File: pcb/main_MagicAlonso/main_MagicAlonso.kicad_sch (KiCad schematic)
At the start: 14 parts, among them J1 XT30PW-M, SW1 SW_SPST, U1 ESP32-WROOM-32E, U2 Mini360, U3 LM1117DT-3.3

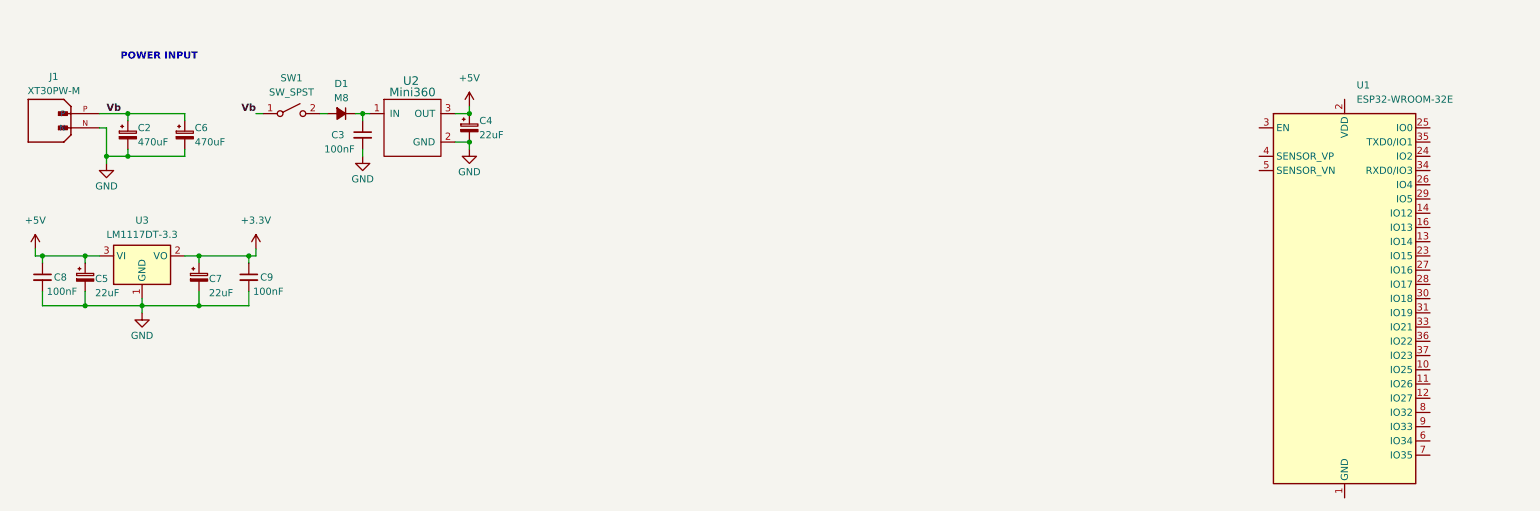
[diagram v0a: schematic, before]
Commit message: Schematic & PCB updates
made advancements on the schematic circuits and the PCB layout drawings.
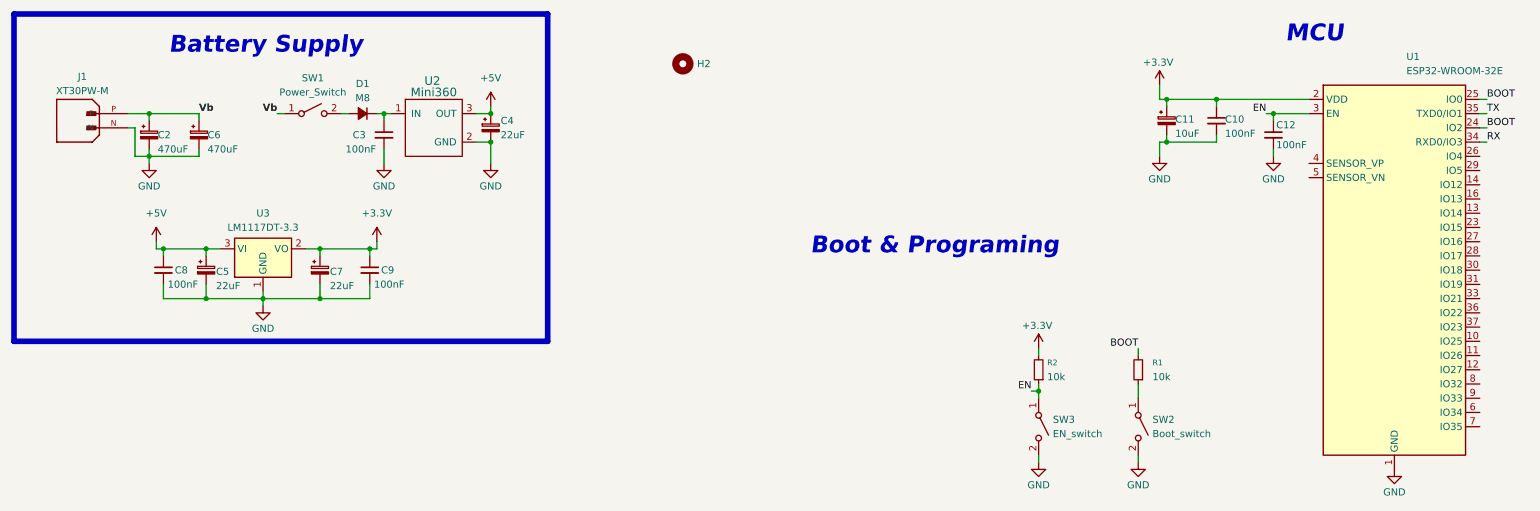
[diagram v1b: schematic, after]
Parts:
- added C10, C12: 100nF, symbol Device:C_Small
- added C11: 10uF, symbol Device:C_Polarized_Small
- added H2: Mounting_Hole, EESTN5:hole_3mm, symbol EESTN5:Mounting_Hole
- added R1, R2: 10k, symbol Device:R_Small
- added SW2: Boot_switch, MixLib:SW_Slide-03_P2.54_L9_W4_H7, symbol Switch:SW_SPST
- added SW3: EN_switch, MixLib:SW_Slide-03_P2.54_L9_W4_H7, symbol Switch:SW_SPST
- SW1: value SW_SPST -> Power_Switch; footprint (none) -> MixLib:SW_Slide-03_P2.54_L9_W4_H7
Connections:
- net +3.3V: now also U1.2 (VDD), C10.1, C11.1, R2.2
- net GND: now also U1.1 (GND), U1.15 (GND), U1.38 (GND), U1.39 (GND), C10.2, C11.2, C12.2, SW2.2 (B), SW3.2 (B)
- net BOOT: now reaches U1.24 (IO2)
- net BOOT: now also U1.25 (IO0), R1.2
- net EN: now reaches U1.3 (EN)
- net EN: now also C12.1, R2.1, SW3.1 (A)
- net RX: now reaches U1.34 (RXD0/IO3)
- net TX: now reaches U1.35 (TXD0/IO1)
- new net: R1.1, SW2.1 (A)
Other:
- note added: "Battery Supply"
- note added: "Boot & Programing"
- note added: "MCU"
- note removed: "POWER INPUT"
- moved on the sheet: C2, C3, C4, C5, C6, C7, C8, C9, D1, J1, SW1, U1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

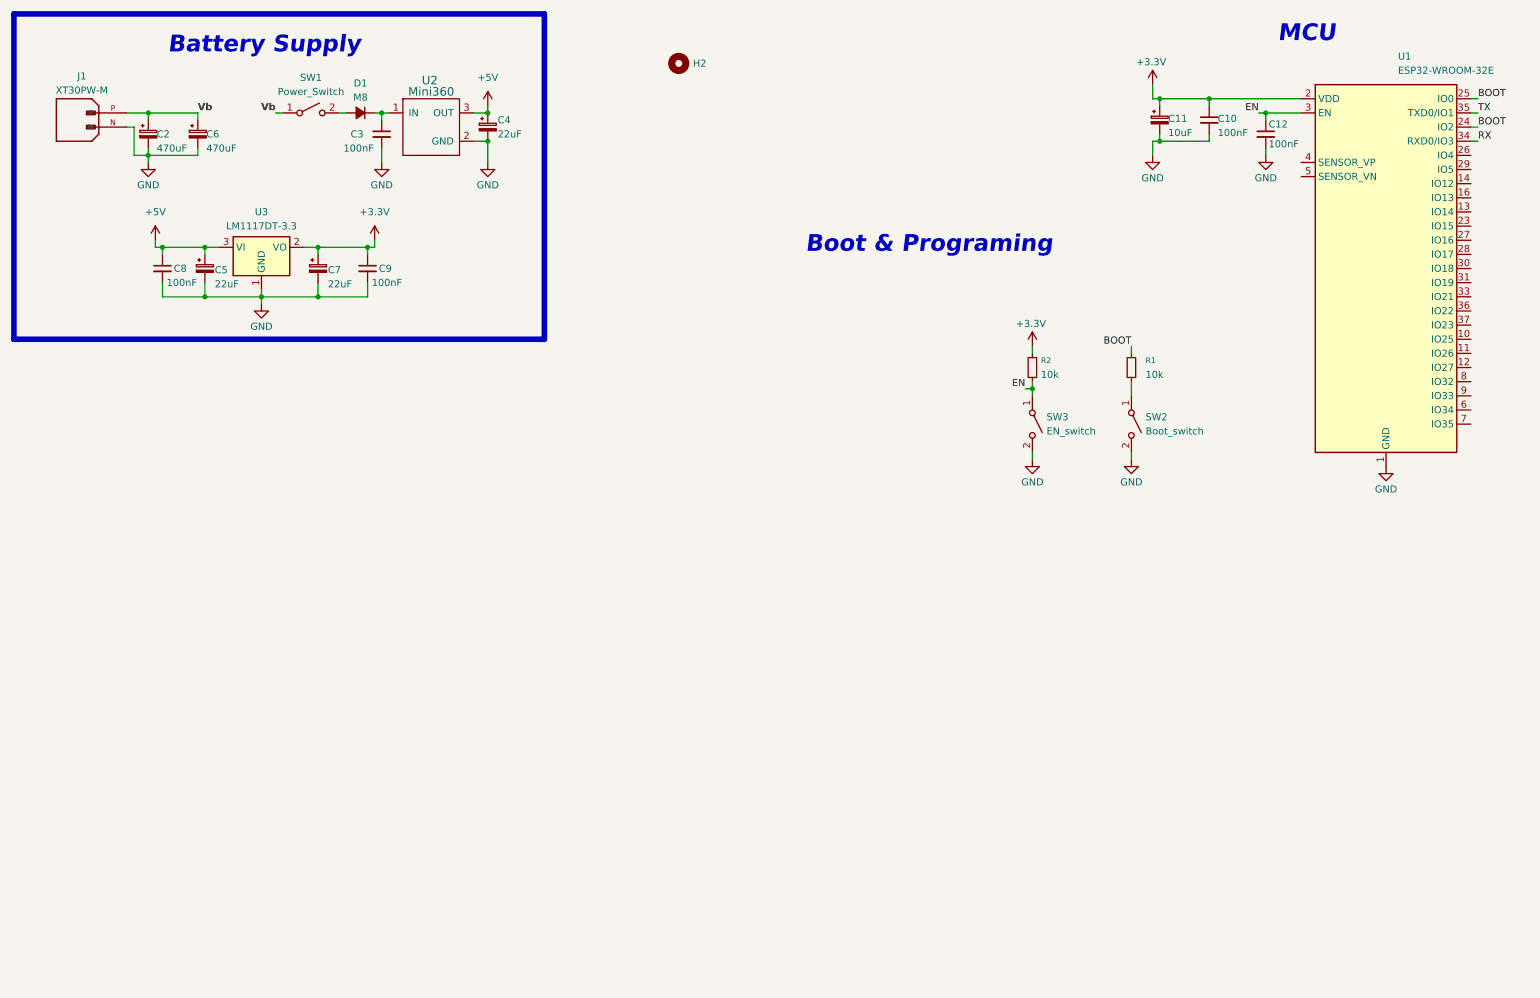
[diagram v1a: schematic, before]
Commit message: more schematic stuff
Added ch340 and some more stuff
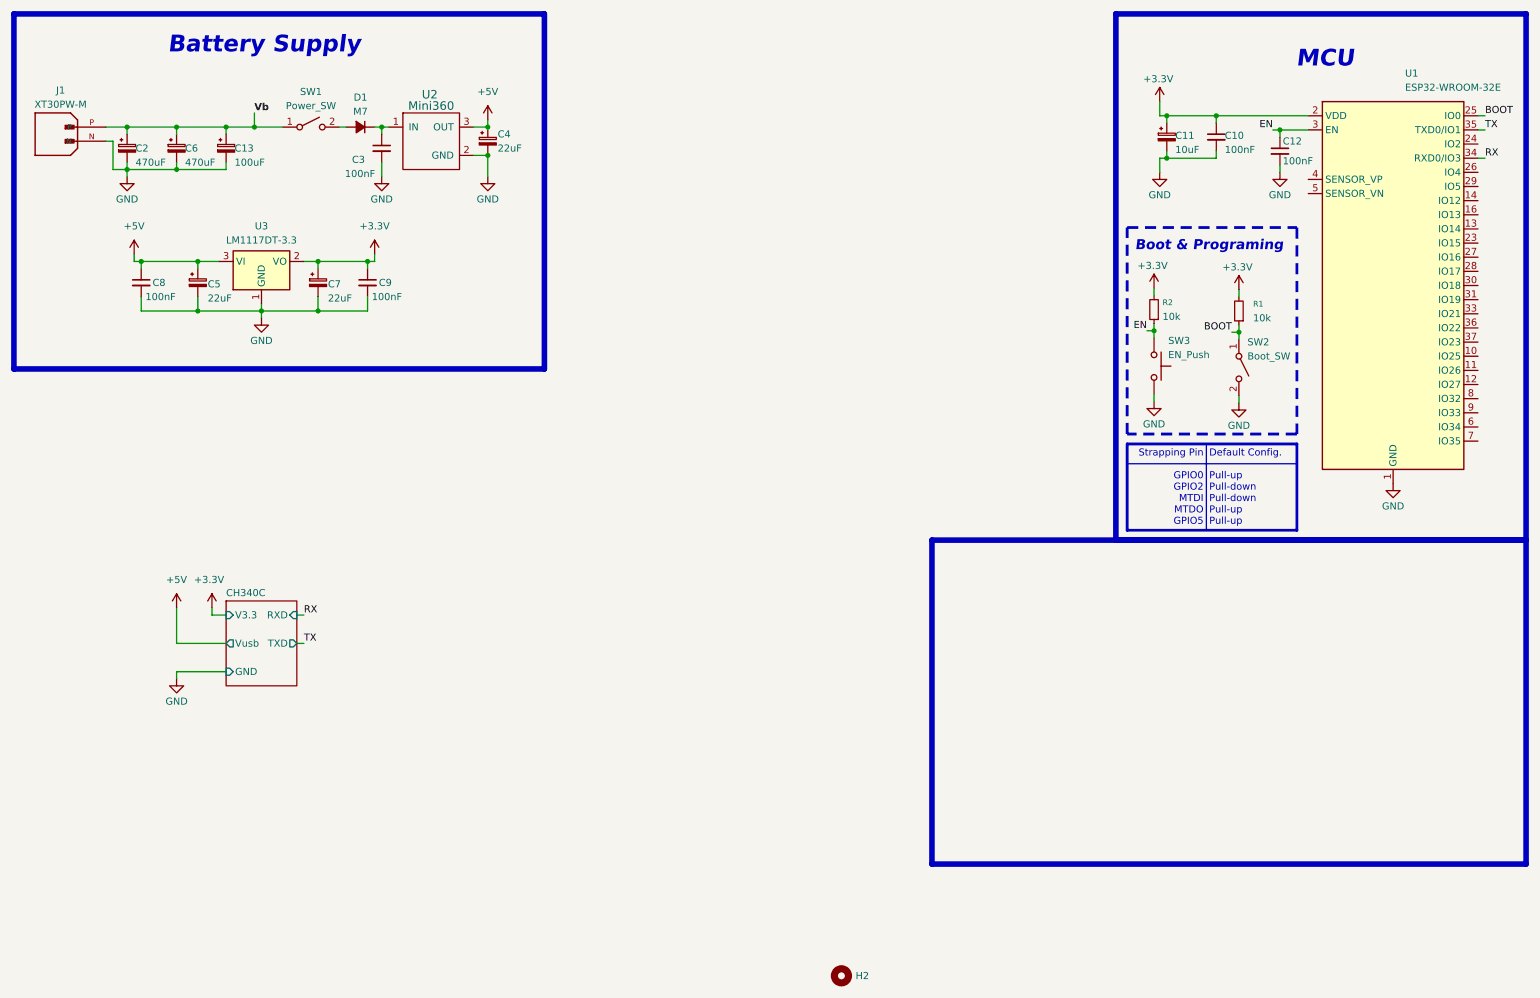
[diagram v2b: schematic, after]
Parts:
- removed SW3: EN_switch, MixLib:SW_Slide-03_P2.54_L9_W4_H7, symbol Switch:SW_SPST
- added C13: 100uF, symbol Device:C_Polarized_Small
- added SW3: EN_Push, symbol Switch:SW_Push
- D1: value M8 -> M7
- SW1: value Power_Switch -> Power_SW
- SW2: value Boot_switch -> Boot_SW
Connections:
- net +3.3V: now also R1.2
- net BOOT: now also R1.1, SW2.1 (A); no longer R1.2, U1.24 (IO2)
- net EN: now also SW3.1
- net GND: now also C13.2, SW3.2
- net Vb: now also C13.1
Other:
- added sheet CH340C (CH340G_programmer.kicad_sch)
- note added: "Default Config. Pull-up Pull-down Pull-down Pull-up Pull-up"
- note added: "Strapping Pin GPIO0 GPIO2 MTDI MTDO GPIO5"
- company: (none) -> JRegi
- title: (none) -> MagicAlonso main control PCB
- moved on the sheet: C10, C11, C12, C2, C3, C4, C5, C6, C7, C8, C9, D1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

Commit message: more schematic
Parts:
- added C17, C18, C19, C20, C21, C22, C23, C24, C25, C26, C27, C28, C29, C30, C31, C32: 100nF, symbol Device:C_Small
- added J5, J6: Conn_01x08_Pin, symbol Connector:Conn_01x08_Pin
- added JP1: JP_ESP, symbol Jumper:SolderJumper_2_Open
- added U5: CD74HC4067, MixLib:HP4067_module, symbol MixLib:CD74HC4067_module
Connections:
- net +3.3V: now also JP1.2 (B); no longer C10.1, C11.1, U1.2 (VDD)
- net GND: now also C17.1, C18.1, C19.1, C20.1, C21.1, C22.1, C23.1, C24.1, C25.1, C26.1, C27.1, C28.1, C29.1, C30.1, C31.1, C32.1, U5.24 (GND)
- net MUX_S1: now reaches U1.6 (IO34)
- net MUX_S1: now also U5.20 (S1)
- net MUX_S0: now reaches U1.7 (IO35)
- net MUX_S0: now also U5.21 (S0)
- net MUX_SIG: now reaches U1.8 (IO32)
- net MUX_SIG: now also U5.17 (SIG)
- new net: C10.1, C11.1, JP1.1 (A), U1.2 (VDD)
- new net MUX_S2: U5.19 (S2)
- new net MUX_S3: U5.18 (S3)
- new net QRE_0: C32.2, J6.8 (Pin_8), U5.16 (C0)
- new net QRE_1: C31.2, J6.7 (Pin_7), U5.15 (C1)
- new net QRE_10: C22.2, J5.6 (Pin_6), U5.6 (C10)
- new net QRE_11: C21.2, J5.5 (Pin_5), U5.5 (C11)
- new net QRE_12: C20.2, J5.4 (Pin_4), U5.4 (C12)
- new net QRE_13: C19.2, J5.3 (Pin_3), U5.3 (C13)
- new net QRE_14: C18.2, J5.2 (Pin_2), U5.2 (C14)
- new net QRE_15: C17.2, J5.1 (Pin_1), U5.1 (C15)
- new net QRE_2: C30.2, J6.6 (Pin_6), U5.14 (C2)
- new net QRE_3: C29.2, J6.5 (Pin_5), U5.13 (C3)
- new net QRE_4: C28.2, J6.4 (Pin_4), U5.12 (C4)
- new net QRE_5: C27.2, J6.3 (Pin_3), U5.11 (C5)
- new net QRE_6: C26.2, J6.2 (Pin_2), U5.10 (C6)
- new net QRE_7: C25.2, J6.1 (Pin_1), U5.9 (C7)
- new net QRE_8: C24.2, J5.8 (Pin_8), U5.8 (C8)
- new net QRE_9: C23.2, J5.7 (Pin_7), U5.7 (C9)
- no-connect marks 0 -> 1
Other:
- note added: "Boot"
- note added: "MUX & Sensors Output"
- note added: "Programming"
- note added: "To-Do - MUX y conexion sensores - giroscopio y acelerometro - encoders - usb-c symbol & footprint - buzzer - 2 LEDs RGB - 1 interface button - mounting holes - ESC connections"
- note removed: "Boot & Programing"
- moved on the sheet: C10, C11, C12, R1, R2, SW2, SW3, U1

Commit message: yes, schematic
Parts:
- added C33, C34: 100nF, symbol Device:C_Small
- C5, C7: value 22uF -> 47uF
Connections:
- net BOOT: now also C34.1
- net EN: now also C33.1
- net GND: now also C33.2, C34.2
- net VDD_ESP: now reaches C10.1, C11.1, JP1.1 (A), U1.2 (VDD)
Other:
- note added: "Interfaces"
- note added: "To-Do - giroscopio y acelerometro - encoders - usb-c symbol & footprint - buzzer - 2 LEDs RGB - 1 interface button - mounting holes - ESC connections"
- note removed: "To-Do - MUX y conexion sensores - giroscopio y acelerometro - encoders - usb-c symbol & footprint - buzzer - 2 LEDs RGB - 1 interface button - mounting holes - ESC connections"
- moved on the sheet: C13, C17, C18, C19, C2, C20, C21, C22, C23, C24, C25, C26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

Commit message: hehe schematic go brr
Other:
- note added: "To-Do - giroscopio y acelerometro - encoders - usb-c symbol & footprint - buzzer - 2 LEDs RGB - 1 interface button - mounting holes - ESC connections - quizas integrar step-down"
- note removed: "To-Do - giroscopio y acelerometro - encoders - usb-c symbol & footprint - buzzer - 2 LEDs RGB - 1 interface button - mounting holes - ESC connections"
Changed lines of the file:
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@@
 		)
 	)
-	(text "To-Do\n- giroscopio y acelerometro\n- encoders\n- usb-c symbol & footprint\n- buzzer\n- 2 LEDs RGB\n- 1 interface button\n- mounting holes\n- ESC connections\n"
+	(text "To-Do\n- giroscopio y acelerometro\n- encoders\n- usb-c symbol & footprint\n- buzzer\n- 2 LEDs RGB\n- 1 interface button\n- mounting holes\n- ESC connections\n- quizas integrar step-down\n"
 		(exclude_from_sim no)
 		(at -114.046 85.598 0)
@@
 			"agA0ACsAbQBrAHcAbgB3AGYAdQBVAHMAcQBrAFIATQB4AE8AYgBTAEgAQQArAHAANQB4AEYARQBk"
 			"AG4ANwBzAEoAbABKAEsASgBGAG8AWgBtAFkAVwBVAHcASwB6AEkAbABBAHQAcgByAGgARgBBAEQA"
-			"dQBmAA=="
+			"dQBmAHoAKwBlAHoAVwBRAGgAQgBzAHUAUwBVAFYAcQB1AFYAOQA1AHgARgBSAEQAVgBVAG8AUQBx"
+			"AGgAYgB1AHEAYwBrAHEAaABlAHUASABEAGgAOAByAFcAcgBKAGUASABlAHEAVABhAGgAUABuAC8A"
+			"dQAvAE8ASABoAGcAWQBpAHEAVwB1AEgAQgB5AHgAUwBGAHEAYQBsAEMAVgBWAFYASABSAC8ATwBj"
+			"AFUAcgAvAHUAbQBxAFoAQgBwAG4ANwBvAGMAOQA3AFkATABoAFQAegBXAFYAQQBwAGcAVgBLAEEA"
+			"QgBBAHkARgA0AGsAUQBFADUAbwAxAGwAUgB3AG0ATwBvADUAMgBGAEIANABCAHoAbgBvAGwAeQB6"
+			"AEQAbABuAFkAaQA3ADkARgAwAEMATABZAEgAawA3AEkASgBRAC8AYgBnAFIARABFAFoARwBaADUA"
+			"bQB6AGIAUgBVAFIAawBSAEgAUgBsADIAdwBhADIARgBhAEkAQwBBAEsAQQBoAGIAQQBlAFIAagBV"
+			"AHMASQBBAEoASQBaADUASQB6ADkASQBCADYAWQBGAFUAVQBNADAAQQBSAFEAbQBRAHgANQBGAE8A"
+			"eABHAFAAVgAwAFAASwBhAHYANwBOAE4ATgB5AEwAMwByAFIAaQArADYANgA2ADYANQA3ADcANwAy"
+			"ADMATABQADcAOAB6AC8ALwA4AHIALwB6AEsAcgAzAFIAZAA5ADUAYQAzAHYARwBYADMAbgBtAGMA"
+			"OQA2ADEAbABmACsANwBWAGYAdQA3AC8AQgAyAEcATwBQAFAAZgBiAFkAWQA0ADgAOQBoAGIAcgBI"
+			"AEgAbgB2AHMAcwBjAGMAZQBlADMAdwBSAEkAVwBmADUAeABMADIAWABQAC8AcgB4AEsAMQBXAG8A"
+			"UQBOAEgAVQBSAEIASwBBAEEAQgBJAGcAQQAzAEwASgBiAEYAbQB2ADEANgB2AFYAZQByAEYAYwBU"
+			"AEIAZQB6AGcANABPAEQAKwBYAHgAZQBOAFgAVgBkADEAUQBRAG8AbwBwAHAAVAA0ADMAbgBvAE8A"
+			"ZwBJAG8ARABvAGsAYgBYADEATQBpAEoAQQBSAEMAQgBpAFEARQBSAGwASgBWADAAVQBRAEEAbABu"
+			"AFAASgB0AFMAOABpAE0AdABpAFMASABVAGgAawBXAC8ANgAwAEUAQgBoAEUAcQBBAG8AUAB0ADYA"
+			"egBkAHMASABUAE0AWABLAHgATABOAHcANgBHAFYASgBLADcAdwBVAFMASwBPAGoATABGAEMAQQBC"
+			"AEYARwA3AHYASgBQAEMASQBpAHAAQwAxADMAeQBwAHUANgA2AFgASABvAGgAMABIAE4AaQBIAGcA"
+			"MgBtAA=="
 		)
 	)

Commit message: schematic go fiuuu
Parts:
- removed C13: 100uF, symbol Device:C_Polarized_Small
- removed C4: 22uF, symbol Device:C_Polarized_Small
- added C35, C39, C40: 100nF, symbol Device:C_Small
- added C36, C37: 47uF, symbol Device:C_Polarized_Small
- C2: value 470uF -> 220uF
- C5, C7: value 47uF -> 22uF
- C6: value 470uF -> 100uF
- J5: value Conn_01x08_Pin -> QRE_Conn1
- J6: value Conn_01x08_Pin -> QRE_Conn2
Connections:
- net +5V: now also C35.1, C36.1
- net GND: now also C35.2, C36.2, C37.2, C39.1, C40.1
- net MUX_SIG: now also C39.2, C40.2
- net at C3.1, D1.1 (K), U2.1 (IN): now also C37.1
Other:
- note added: "To-Do - giroscopio y acelerometro - encoders - usb-c symbol & footprint - buzzer - 2 LEDs RGB - 1 interface button - DIP Switch 2 vias - mounting holes - ESC connections - quizas integrar step-down"
- note removed: "To-Do - giroscopio y acelerometro - encoders - usb-c symbol & footprint - buzzer - 2 LEDs RGB - 1 interface button - mounting holes - ESC connections - quizas integrar step-down"
- moved on the sheet: C17, C18, C19, C20, C21, C22, C23, C24, C25, C26, C27, C28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

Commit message: esquematico
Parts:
- removed C17, C18, C19, C20, C21, C22, C23, C24, C25, C26, C27, C28, C29, C30, C31, C32, C39, C40: 100nF, symbol Device:C_Small
- added C13: 1uF, symbol Device:C_Polarized_Small
- added C38: 100nF, symbol Device:C_Small
- added R7: 10k, symbol Device:R_Small
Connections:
- net +3.3V: now also U5.23 (VCC), C13.1, C38.1
- net GND: now also C13.2, C38.2, R7.1
- net MUX_SIG: now also R7.2
- net +5V renamed +4.3
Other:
- moved on the sheet: C3, C35, C36, C37, C5, C7, C8, C9, D1, SW1, U2, U3

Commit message: esquematico
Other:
- note added: "To-Do - giroscopio y acelerometro - encoders - usb module footprint - buzzer - 2 ws2822b smd - 1 interface button - DIP Switch 2 vias ?? - mounting holes - ESC connections - quizas integrar step-down - soldar modulo de MUX como Modulo SMD - Sensores de corriente"
- note removed: "To-Do - giroscopio y acelerometro - encoders - usb-c symbol & footprint - buzzer - 2 LEDs RGB - 1 interface button - DIP Switch 2 vias - mounting holes - ESC connections - quizas integrar step-down"
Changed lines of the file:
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@@
 		)
 	)
-	(text "To-Do\n- giroscopio y acelerometro\n- encoders\n- usb-c symbol & footprint\n- buzzer\n- 2 LEDs RGB\n- 1 interface button\n- DIP Switch 2 vias\n- mounting holes\n- ESC connections\n- quizas integrar step-down\n"
+	(text "To-Do\n- giroscopio y acelerometro\n- encoders\n- usb module footprint\n- buzzer\n- 2 ws2822b smd\n- 1 interface button\n- DIP Switch 2 vias ??\n- mounting holes\n- ESC connections\n- quizas integrar step-down\n- soldar modulo de MUX como Modulo SMD\n- Sensores de corriente"
 		(exclude_from_sim no)
-		(at -114.046 85.598 0)
+		(at -167.894 75.184 0)
 		(effects
 			(font
@@
 	(text "Interfaces"
 		(exclude_from_sim no)
-		(at 146.05 142.494 0)
+		(at 129.794 142.748 0)
 		(effects
 			(font
@@
 			"RAA5AHgAMgAyADAAVwBvADEAaQB1AHYAdgBQAEkAVgByADMAagBGAHoAVABmAGYAZgBNAHMAdAB0"
 			"AC8AQQBZAFgAdgByAFMAbAAyADYAMwBXADgAWgBGAHYAMwBRADkAKwBlAFMAVAA5ADkAeAB6AHoA"
-			"NQBWAA=="
+			"NQBWADQAUQAzAEQAZwBEAGQALwBVAG8AagBkADkARwBQAGUAeABxACsAdgBQAE8AYQBzAEkASQBu"
+			"AHEALwBpAFQAWQBxAHgAZgB2AE8AdQBZADAATwBUAGwAWABNAFEARQBCAEUAaAByADYAUABLAGMA"
+			"YQBVAG0ATABtAHEAYQB6AFcATgBTAGEAVQBJADgAVQBLAFkAVABDAGEANgBrAFgAdwBDACsAMgBB"
+			"AEEAagB0AGwANQBMADEAbQBHAGsAdABoAE8AdQBQAFYAZABoAEMAeQBxAGEAbQAzAGIAQgB1ACsA"
+			"ZABZAHoAVQBMAEkAWQBRAFEAQwBzAHMAVwBZADEAeQB2ADEAegA2AEUAdABtAGwARQBwAEQAQgBs"
+			"ADUAYQBlAGsARwBFAHUAYQBVAHcAaQBoAGUATwBlAFYAUwBDAGcAdwA2AC8AcAArAHMAVgBoADAA"
+			"WABUAGUAYgB6AFcASQBmAFYAZABWADUAQgB5AFAARQBHAE0ASABzAHcAcwBXAEwAeABYAEMAVABt"
+			"AGIAMwBmAEYAQgA4AGoAZwB2AFAAYwBUAGkAYgBCACsAOQBQAEYAWQByAGwAYwB6AFcAYgB6AHQA"
+			"bQAwAFgAaQAxAE8AbQBEAFgAKwA4AHEAMwBwAFcAdABaAEwAdABUAGsAUQBoAGgATQBLAGcAaQBR"
+			"AGcAVABlAGUAWQBjAEkAdwBMAFcAbwBaAEsAYwBIAGIATgBqAEoAawBRAFIAeQBUAGwANQBEAE8A"
+			"UQBvAHAAUQBRAEcASgBTAEUASwBFAEYAUwBrADYAUAB1AHEAcQBsAEkAZAB2AFAAZABWAFYAUQBP"
+			"AE0AaQBPAGoAWQBHAFEARQBBAEIARgArAFoAZwBZAHEAVwB5AEMAWQBSAFUAZABPAGMAQgBaAEUA"
+			"SQBLAFcAYwBGAEEAMgBaAFgAZgBGAHEAWgBIAFMAQgB3AEMASQBYAFUARwA0AFkAaAA1AFYAeQBj"
+			"AEYAbwBnAG8ATwBEACsAYgBUAGsAKwBYAEMAegBNAEQAdwBPAEQAOQBmAEQAWQA3AG4AQgA4AHcA"
+			"OAAzAHIAbwBBAGEAQQBVADUAZwBmAHYAaQBIAGkAagBtAFUAWAAwAFAAbwBUAGcAdgBmAGMAeAB4"
+			"AG4ARQBjAGkAWgB1ADYAcgByAE4ASQB6AG4AawAyAG4AYQA2AFgAcQB6AEcAbABjAGgAbwBHADUA"
+			"eQBlAFQAOQB2AGoANABtAEIAQwA2AHIAdQB1ADYAVABsAFgAcgB1AHEAbgBxAEEAQQBRAGkAawBu"
+			"AE8ATwBNAFgAbgB5AGIAVABzAHAARwBVADEAOQBQAHoAcgBuAG0AbQBiAGkAWABEAGcAOQBQAFQA"
+			"MAA2AA=="
 		)
 	)
@@
 		)
 		(property "Value" "100nF"
-			(at 234.188 38.608 0)
+			(at 235.458 38.608 0)
 			(effects
 				(font
